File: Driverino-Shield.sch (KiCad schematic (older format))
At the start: 56 parts, among them P1 Power, P10 MOT, P11 HALL, P2 Analog, P3 Digital, P4 Digital, P5 CONN_01X01, P6 CONN_01X01, P7 CONN_01X01, P8 CONN_01X01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

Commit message: Update BOM
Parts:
- JP1: RS (none) -> 180-0478
- JP2: RS (none) -> 180-0534
- P11: RS (none) -> 279-9241
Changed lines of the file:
@@
 F 6 "Molex" H 15100 6950 50  0001 C CNN "Manufacturer"
 F 7 "538-53047-0810" H 15100 6950 50  0001 C CNN "Mouser"
+F 8 "279-9241" H 15100 6950 50  0001 C CNN "RS"
 	1    15100 6950
 	1    0    0    1
@@
 F 6 "Samtec" H 14700 5700 50  0001 C CNN "Manufacturer"
 F 7 "200-TMS10301GS" H 14700 5700 50  0001 C CNN "Mouser"
+F 8 "180-0478" H 14700 5700 50  0001 C CNN "RS"
 	1    14700 5700
 	1    0    0    -1
@@
 F 6 "Samtec" H 12250 4625 50  0001 C CNN "Manufacturer"
 F 7 "200-TMS10201GS" H 12250 4625 50  0001 C CNN "Mouser"
+F 8 "180-0534" H 12250 4625 50  0001 C CNN "RS"
 	1    12250 4625
 	1    0    0    -1

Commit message: Update BOM
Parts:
- C1: Digikey (none) -> 399-7444-1-ND
- C10, C11, C12, C4: Digikey (none) -> 445-6901-1-ND
- C2: Digikey (none) -> P124837CT-ND
- C3: Digikey (none) -> 445-172483-1-ND
- C5, C7: Digikey (none) -> 311-2082-1-ND
- C6: Digikey (none) -> 490-4762-1-ND
- C8, C9: Digikey (none) -> 445-5666-1-ND
- D1: Digikey (none) -> 475-2486-1-ND
- D2: Digikey (none) -> LBQ39G-N1OO-35-1-ND
- D3: Digikey (none) -> 475-3442-1-ND
- D5: Digikey (none) -> TSZU52C5V1RGG-ND
- F1: Digikey (none) -> 118-MF-ASML020/6-2DKR-ND
- JP1: Digikey (none) -> SAM10238-ND
- JP2: Digikey (none) -> SAM12199-ND
- L1: Digikey (none) -> CBC3225T470KRV
- P1, P4: Digikey (none) -> SSW-108-03-G-S-ND
- P10: Digikey (none) -> 0397730003-ND
- P11: Digikey (none) -> WM1737-ND
- P2: Digikey (none) -> SSW-106-03-G-S-ND
- P3: Digikey (none) -> SSW-110-03-G-S-ND
- P9: Digikey (none) -> 0397730002-ND
- R1, R13, R3, R5, R7, R8: Digikey (none) -> 541-3949-1-ND
- R10, R11, R12, R14, R15, R16, R17, R9: Digikey (none) -> 541-4013-1-ND
- R18, R19, R20, R21, R22, R23: Digikey (none) -> 541-3958-1-ND
- R2, R4, R6: Digikey (none) -> ESR03EZPF5101-ND

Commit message: Update BOM
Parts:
- C1: Farnell (none) -> 2118135RL
- C10, C11, C12, C4: Farnell (none) -> 2210830
- C2: Farnell (none) -> 3126986
- C3: Farnell (none) -> 2547055
- C5, C7: Farnell (none) -> 2211179
- C6: Farnell (none) -> 2470416
- C8, C9: Farnell (none) -> 2346967
- D4: Farnell (none) -> 2463989
- F1: Farnell (none) -> 3350793
- JP1: Farnell (none) -> 2856614
- JP2: Farnell (none) -> 2505048
- P11: Farnell (none) -> 1012258
- P3: Farnell (none) -> 3661270
- R18, R19, R20, R21, R22, R23: Farnell (none) -> 2616725
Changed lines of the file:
@@
 F 7 "200-SSW11003GS" H 14850 1600 50  0001 C CNN "Mouser"
 F 8 "SSW-110-03-G-S-ND" H 14850 1600 50  0001 C CNN "Digikey"
+F 9 "3661270" H 14850 1600 50  0001 C CNN "Farnell"
 	1    14850 1600
 	-1   0    0    -1
@@
 F 8 "81-GCM155R71H103KA5D" H 5150 4725 50  0001 C CNN "Mouser"
 F 9 "490-4762-1-ND" H 5150 4725 50  0001 C CNN "Digikey"
+F 10 "2470416" H 5150 4725 50  0001 C CNN "Farnell"
 	1    5150 4725
 	0    1    1    0
@@
 F 8 "603-CC603KRX7R9BB105" H 4475 4825 50  0001 C CNN "Mouser"
 F 9 "311-2082-1-ND" H 4475 4825 50  0001 C CNN "Digikey"
+F 10 "2211179" H 4475 4825 50  0001 C CNN "Farnell"
 	1    4475 4825
 	0    1    1    0
@@
 F 8 "810-CGA5L1X7R1V106KE" H 4075 5450 50  0001 C CNN "Mouser"
 F 9 "	445-172483-1-ND" H 4075 5450 50  0001 C CNN "Digikey"
+F 10 "2547055" H 4075 5450 50  0001 C CNN "Farnell"
 	1    4075 5450
 	-1   0    0    1
@@
 F 8 "810-CGA2B3X7R1V104K" H 4475 5450 50  0001 C CNN "Mouser"
 F 9 "445-6901-1-ND" H 4475 5450 50  0001 C CNN "Digikey"
+F 10 "2210830" H 4475 5450 50  0001 C CNN "Farnell"
 	1    4475 5450
 	-1   0    0    1
@@
 F 7 "667-EEE-FTV151XAV" H 3800 5450 50  0001 C CNN "Mouser"
 F 8 "	P124837CT-ND" H 3800 5450 50  0001 C CNN "Digikey"
+F 9 "	3126986" H 3800 5450 50  0001 C CNN "Farnell"
 	1    3800 5450
 	1    0    0    -1
@@
 F 8 "603-CC603KRX7R9BB105" H 7750 4825 50  0001 C CNN "Mouser"
 F 9 "311-2082-1-ND" H 7750 4825 50  0001 C CNN "Digikey"
+F 10 "2211179" H 7750 4825 50  0001 C CNN "Farnell"
 	1    7750 4825
 	0    -1   -1   0
@@
 F 9 "810-CGA2B3X7R1V104K" H 13050 6425 50  0001 C CNN "Mouser"
 F 10 "445-6901-1-ND" H 13050 6425 50  0001 C CNN "Digikey"
+F 11 "2210830" H 13050 6425 50  0001 C CNN "Farnell"
 	1    13050 6425
 	-1   0    0    1
@@
 F 9 "810-CGA2B3X7R1V104K" H 13050 6950 50  0001 C CNN "Mouser"
 F 10 "445-6901-1-ND" H 13050 6950 50  0001 C CNN "Digikey"
+F 11 "2210830" H 13050 6950 50  0001 C CNN "Farnell"
 	1    13050 6950
 	-1   0    0    1
@@
 F 9 "810-CGA2B3X7R1V104K" H 13050 7475 50  0001 C CNN "Mouser"
 F 10 "445-6901-1-ND" H 13050 7475 50  0001 C CNN "Digikey"
+F 11 "2210830" H 13050 7475 50  0001 C CNN "Farnell"
 	1    13050 7475
 	-1   0    0    1
@@
 F 7 "652-MF-ASML020/6-2" H 3150 8700 50  0001 C CNN "Mouser"
 F 8 "118-MF-ASML020/6-2DKR-ND" H 3150 8700 50  0001 C CNN "Digikey"
+F 9 "3350793" H 3150 8700 50  0001 C CNN "Farnell"
 	1    3150 8700
 	1    0    0    -1
@@
 F 8 "80-C1206C226M8R" H 3575 9075 50  0001 C CNN "Mouser"
 F 9 "	399-7444-1-ND" H 3575 9075 50  0001 C CNN "Digikey"
+F 10 "2118135RL" H 3575 9075 50  0001 C CNN "Farnell"
 	1    3575 9075
 	-1   0    0    1
@@
 F 6 "Kingbright " H 6650 9200 50  0001 C CNN "Manufacturer"
 F 7 "466-3728" H 6650 9200 50  0001 C CNN "RS"
+F 8 "2463989" H 6650 9200 50  0001 C CNN "Farnell"
 	1    6650 9200
 	0    1    1    0
@@
 F 8 "279-9241" H 15100 6950 50  0001 C CNN "RS"
 F 9 "WM1737-ND" H 15100 6950 50  0001 C CNN "Digikey"
+F 10 "1012258" H 15100 6950 50  0001 C CNN "Farnell"
 	1    15100 6950
 	1    0    0    1
@@
 F 8 "71-CRCW040210K0JNEDC" H 14225 7550 50  0001 C CNN "Mouser"
 F 9 "541-3958-1-ND" H 14225 7550 50  0001 C CNN "Digikey"
+F 10 "2616725" H 14225 7550 50  0001 C CNN "Farnell"
 	1    14225 7550
 	1    0    0    -1
@@
 F 8 "71-CRCW040210K0JNEDC" H 13950 7550 50  0001 C CNN "Mouser"
 F 9 "541-3958-1-ND" H 13950 7550 50  0001 C CNN "Digikey"
+F 10 "2616725" H 13950 7550 50  0001 C CNN "Farnell"
 	1    13950 7550
 	1    0    0    -1
@@
 F 8 "71-CRCW040210K0JNEDC" H 14500 7550 50  0001 C CNN "Mouser"
 F 9 "541-3958-1-ND" H 14500 7550 50  0001 C CNN "Digikey"
+F 10 "2616725" H 14500 7550 50  0001 C CNN "Farnell"
 	1    14500 7550
 	1    0    0    -1
@@
 F 8 "71-CRCW040210K0JNEDC" H 14500 6275 50  0001 C CNN "Mouser"
 F 9 "541-3958-1-ND" H 14500 6275 50  0001 C CNN "Digikey"
+F 10 "2616725" H 14500 6275 50  0001 C CNN "Farnell"
 	1    14500 6275
 	1    0    0    1
@@
 F 8 "71-CRCW040210K0JNEDC" H 14225 6275 50  0001 C CNN "Mouser"
 F 9 "541-3958-1-ND" H 14225 6275 50  0001 C CNN "Digikey"
+F 10 "2616725" H 14225 6275 50  0001 C CNN "Farnell"
 	1    14225 6275
 	1    0    0    1
@@
 F 8 "71-CRCW040210K0JNEDC" H 13950 6275 50  0001 C CNN "Mouser"
 F 9 "541-3958-1-ND" H 13950 6275 50  0001 C CNN "Digikey"
+F 10 "2616725" H 13950 6275 50  0001 C CNN "Farnell"
 	1    13950 6275
 	1    0    0    1
@@
 F 8 "10-CGA3E2X7R1H104K" H 8625 9075 50  0001 C CNN "Mouser"
 F 9 "445-5666-1-ND" H 8625 9075 50  0001 C CNN "Digikey"
+F 10 "2346967" H 8625 9075 50  0001 C CNN "Farnell"
 	1    8625 9075
 	-1   0    0    1
@@
 F 8 "10-CGA3E2X7R1H104K" H 10450 9075 50  0001 C CNN "Mouser"
 F 9 "445-5666-1-ND" H 10450 9075 50  0001 C CNN "Digikey"
+F 10 "2346967" H 10450 9075 50  0001 C CNN "Farnell"
 	1    10450 9075
 	-1   0    0    1
@@
 F 8 "180-0478" H 14700 5700 50  0001 C CNN "RS"
 F 9 "	SAM10238-ND" H 14700 5700 50  0001 C CNN "Digikey"
+F 10 "2856614" H 14700 5700 50  0001 C CNN "Farnell"
 	1    14700 5700
 	1    0    0    -1
@@
 F 8 "180-0534" H 12250 4625 50  0001 C CNN "RS"
 F 9 "SAM12199-ND" H 12250 4625 50  0001 C CNN "Digikey"
+F 10 "2505048" H 12250 4625 50  0001 C CNN "Farnell"
 	1    12250 4625
 	1    0    0    -1

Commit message: Update BOM
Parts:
- C2: manufacturer1 (none) -> Panasonic; mpn1 (none) -> EEEFTV151XAP
- D4: manufacturer1 (none) -> OSRAM Opto; mpn1 (none) -> LS Q976-NR-1
- D5: RS (none) -> 796-5676; manufacturer1 (none) -> Taiwan Semiconductor; mpn1 (none) -> BZT52C5V1K RKG
- P1, P4: RS (none) -> 180-0432; manufacturer1 (none) -> Samtec; mpn1 (none) -> SSW-108-03-T-S
- P2: RS (none) -> 180-0391; manufacturer1 (none) -> Samtec; mpn1 (none) -> SSW-106-03-T-S
- P3: RS (none) -> 207-9189; manufacturer1 (none) -> Samtec; mpn1 (none) -> SSW-110-03-T-S
- R1, R13, R3, R5, R7, R8: RS (none) -> 678-9875
- R10, R11, R12, R14, R15, R16, R17, R9: RS (none) -> 678-9670
- R18, R19, R20, R21, R22, R23: RS (none) -> 812-1723; manufacturer1 (none) -> Vishay; mpn1 (none) -> CRCW040210K0JNEDIF
- R2, R4, R6: RS (none) -> 679-0566; manufacturer1 (none) -> Vishay; mpn1 (none) -> CRCW06035K10FKEA
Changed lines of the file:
@@
 F 7 "200-SSW10803GS" H 14450 1900 50  0001 C CNN "Mouser"
 F 8 "SSW-108-03-G-S-ND" H 14450 1900 50  0001 C CNN "Digikey"
+F 9 "180-0432" H 14450 1900 50  0001 C CNN "RS"
+F 10 "Samtec" H 14450 1900 50  0001 C CNN "manufacturer1"
+F 11 "SSW-108-03-T-S" H 14450 1900 50  0001 C CNN "mpn1"
 	1    14450 1900
 	1    0    0    -1
@@
 F 7 "200-SSW10603GS" H 14450 2700 50  0001 C CNN "Mouser"
 F 8 "SSW-106-03-G-S-ND" H 14450 2700 50  0001 C CNN "Digikey"
+F 9 "180-0391" H 14450 2700 50  0001 C CNN "RS"
+F 10 "Samtec" H 14450 2700 50  0001 C CNN "manufacturer1"
+F 11 "SSW-106-03-T-S" H 14450 2700 50  0001 C CNN "mpn1"
 	1    14450 2700
 	1    0    0    -1
@@
 F 7 "200-SSW10803GS" H 14850 2600 50  0001 C CNN "Mouser"
 F 8 "SSW-108-03-G-S-ND" H 14850 2600 50  0001 C CNN "Digikey"
+F 9 "180-0432" H 14850 2600 50  0001 C CNN "RS"
+F 10 "Samtec" H 14850 2600 50  0001 C CNN "manufacturer1"
+F 11 "SSW-108-03-T-S" H 14850 2600 50  0001 C CNN "mpn1"
 	1    14850 2600
 	-1   0    0    -1
@@
 F 8 "SSW-110-03-G-S-ND" H 14850 1600 50  0001 C CNN "Digikey"
 F 9 "3661270" H 14850 1600 50  0001 C CNN "Farnell"
+F 10 "207-9189" H 14850 1600 50  0001 C CNN "RS"
+F 11 "Samtec" H 14850 1600 50  0001 C CNN "manufacturer1"
+F 12 "SSW-110-03-T-S" H 14850 1600 50  0001 C CNN "mpn1"
 	1    14850 1600
 	-1   0    0    -1
@@
 F 7 "755-ESR03EZPF5101" H 6925 2975 50  0001 C CNN "Mouser"
 F 8 "	ESR03EZPF5101-ND" H 6925 2975 50  0001 C CNN "Digikey"
+F 9 "679-0566" H 6925 2975 50  0001 C CNN "RS"
+F 10 "Vishay" H 6925 2975 50  0001 C CNN "manufacturer1"
+F 11 "CRCW06035K10FKEA" H 6925 2975 50  0001 C CNN "mpn1"
 	1    6925 2975
 	1    0    0    -1
@@
 F 8 "	P124837CT-ND" H 3800 5450 50  0001 C CNN "Digikey"
 F 9 "	3126986" H 3800 5450 50  0001 C CNN "Farnell"
+F 10 "Panasonic" H 3800 5450 50  0001 C CNN "manufacturer1"
+F 11 "EEEFTV151XAP" H 3800 5450 50  0001 C CNN "mpn1"
 	1    3800 5450
 	1    0    0    -1
@@
 F 7 "755-ESR03EZPF5101" H 5675 2975 50  0001 C CNN "Mouser"
 F 8 "	ESR03EZPF5101-ND" H 5675 2975 50  0001 C CNN "Digikey"
+F 9 "679-0566" H 5675 2975 50  0001 C CNN "RS"
+F 10 "Vishay" H 5675 2975 50  0001 C CNN "manufacturer1"
+F 11 "CRCW06035K10FKEA" H 5675 2975 50  0001 C CNN "mpn1"
 	1    5675 2975
 	-1   0    0    -1
@@
 F 7 "71-CRCW06031K00FKEAC" H 5200 8625 50  0001 C CNN "Mouser"
 F 8 "541-3949-1-ND" H 5200 8625 50  0001 C CNN "Digikey"
+F 9 "678-9875" H 5200 8625 50  0001 C CNN "RS"
 	1    5200 8625
 	1    0    0    -1
@@
 F 7 "71-CRCW06031K00FKEAC" H 5675 8625 50  0001 C CNN "Mouser"
 F 8 "541-3949-1-ND" H 5675 8625 50  0001 C CNN "Digikey"
+F 9 "678-9875" H 5675 8625 50  0001 C CNN "RS"
 	1    5675 8625
 	1    0    0    -1
@@
 F 7 "755-ESR03EZPF5101" H 6150 8625 50  0001 C CNN "Mouser"
 F 8 "	ESR03EZPF5101-ND" H 6150 8625 50  0001 C CNN "Digikey"
+F 9 "679-0566" H 6150 8625 50  0001 C CNN "RS"
+F 10 "Vishay" H 6150 8625 50  0001 C CNN "manufacturer1"
+F 11 "CRCW06035K10FKEA" H 6150 8625 50  0001 C CNN "mpn1"
 	1    6150 8625
 	1    0    0    -1
@@
 F 7 "71-CRCW06031K00FKEAC" H 6650 8625 50  0001 C CNN "Mouser"
 F 8 "541-3949-1-ND" H 6650 8625 50  0001 C CNN "Digikey"
+F 9 "678-9875" H 6650 8625 50  0001 C CNN "RS"
 	1    6650 8625
 	1    0    0    -1
@@
 F 7 "466-3728" H 6650 9200 50  0001 C CNN "RS"
 F 8 "2463989" H 6650 9200 50  0001 C CNN "Farnell"
+F 9 "OSRAM Opto" H 6650 9200 50  0001 C CNN "manufacturer1"
+F 10 "LS Q976-NR-1" H 6650 9200 50  0001 C CNN "mpn1"
 	1    6650 9200
 	0    1    1    0
@@
 F 7 "71-CRCW06030000Z0EBC" H 13875 4625 50  0001 C CNN "Mouser"
 F 8 "541-4013-1-ND" H 13875 4625 50  0001 C CNN "Digikey"
+F 9 "678-9670" H 13875 4625 50  0001 C CNN "RS"
 	1    13875 4625
 	0    1    1    0
@@
 F 9 "541-3958-1-ND" H 14225 7550 50  0001 C CNN "Digikey"
 F 10 "2616725" H 14225 7550 50  0001 C CNN "Farnell"
+F 11 "812-1723" H 14225 7550 50  0001 C CNN "RS"
+F 12 "Vishay" H 14225 7550 50  0001 C CNN "manufacturer1"
+F 13 "CRCW040210K0JNEDIF" H 14225 7550 50  0001 C CNN "mpn1"
 	1    14225 7550
 	1    0    0    -1
@@
 F 9 "541-3958-1-ND" H 13950 7550 50  0001 C CNN "Digikey"
 F 10 "2616725" H 13950 7550 50  0001 C CNN "Farnell"
+F 11 "812-1723" H 13950 7550 50  0001 C CNN "RS"
+F 12 "Vishay" H 13950 7550 50  0001 C CNN "manufacturer1"
+F 13 "CRCW040210K0JNEDIF" H 13950 7550 50  0001 C CNN "mpn1"
 	1    13950 7550
 	1    0    0    -1
@@
 F 9 "541-3958-1-ND" H 14500 7550 50  0001 C CNN "Digikey"
 F 10 "2616725" H 14500 7550 50  0001 C CNN "Farnell"
+F 11 "812-1723" H 14500 7550 50  0001 C CNN "RS"
+F 12 "Vishay" H 14500 7550 50  0001 C CNN "manufacturer1"
+F 13 "CRCW040210K0JNEDIF" H 14500 7550 50  0001 C CNN "mpn1"
 	1    14500 7550
 	1    0    0    -1
@@
 F 9 "541-3958-1-ND" H 14500 6275 50  0001 C CNN "Digikey"
 F 10 "2616725" H 14500 6275 50  0001 C CNN "Farnell"
+F 11 "812-1723" H 14500 6275 50  0001 C CNN "RS"
+F 12 "Vishay" H 14500 6275 50  0001 C CNN "manufacturer1"
+F 13 "CRCW040210K0JNEDIF" H 14500 6275 50  0001 C CNN "mpn1"
 	1    14500 6275
 	1    0    0    1
@@
 F 9 "541-3958-1-ND" H 14225 6275 50  0001 C CNN "Digikey"
 F 10 "2616725" H 14225 6275 50  0001 C CNN "Farnell"
+F 11 "812-1723" H 14225 6275 50  0001 C CNN "RS"
+F 12 "Vishay" H 14225 6275 50  0001 C CNN "manufacturer1"
+F 13 "CRCW040210K0JNEDIF" H 14225 6275 50  0001 C CNN "mpn1"
 	1    14225 6275
 	1    0    0    1
@@
 F 9 "541-3958-1-ND" H 13950 6275 50  0001 C CNN "Digikey"
 F 10 "2616725" H 13950 6275 50  0001 C CNN "Farnell"
+F 11 "812-1723" H 13950 6275 50  0001 C CNN "RS"
+F 12 "Vishay" H 13950 6275 50  0001 C CNN "manufacturer1"
+F 13 "CRCW040210K0JNEDIF" H 13950 6275 50  0001 C CNN "mpn1"
 	1    13950 6275
 	1    0    0    1
@@
 F 7 "71-CRCW06031K00FKEAC" H 8300 9075 50  0001 C CNN "Mouser"
 F 8 "541-3949-1-ND" H 8300 9075 50  0001 C CNN "Digikey"
+F 9 "678-9875" H 8300 9075 50  0001 C CNN "RS"
 	1    8300 9075
 	1    0    0    -1
@@
 F 7 "71-CRCW06031K00FKEAC" H 7950 8700 50  0001 C CNN "Mouser"
 F 8 "541-3949-1-ND" H 7950 8700 50  0001 C CNN "Digikey"
+F 9 "678-9875" H 7950 8700 50  0001 C CNN "RS"
 	1    7950 8700
 	0    1    1    0
@@
 F 7 "71-CRCW06031K00FKEAC" H 10100 8700 50  0001 C CNN "Mouser"
 F 8 "541-3949-1-ND" H 10100 8700 50  0001 C CNN "Digikey"
+F 9 "678-9875" H 10100 8700 50  0001 C CNN "RS"
 	1    10100 8700
 	0    1    1    0
@@
 F 7 "71-CRCW06030000Z0EBC" H 10200 4850 50  0001 C CNN "Mouser"
 F 8 "541-4013-1-ND" H 10200 4850 50  0001 C CNN "Digikey"
+F 9 "678-9670" H 10200 4850 50  0001 C CNN "RS"
 	1    10200 4850
 	0    1    1    0
@@
 F 7 "71-CRCW06030000Z0EBC" H 10200 4550 50  0001 C CNN "Mouser"
 F 8 "541-4013-1-ND" H 10200 4550 50  0001 C CNN "Digikey"
+F 9 "678-9670" H 10200 4550 50  0001 C CNN "RS"
 	1    10200 4550
 	0    1    1    0
@@
 F 7 "71-CRCW06030000Z0EBC" H 10200 5150 50  0001 C CNN "Mouser"
 F 8 "541-4013-1-ND" H 10200 5150 50  0001 C CNN "Digikey"
+F 9 "678-9670" H 10200 5150 50  0001 C CNN "RS"
 	1    10200 5150
 	0    1    1    0
@@
 F 7 "71-CRCW06030000Z0EBC" H 10200 5800 50  0001 C CNN "Mouser"
 F 8 "541-4013-1-ND" H 10200 5800 50  0001 C CNN "Digikey"
+F 9 "678-9670" H 10200 5800 50  0001 C CNN "RS"
 	1    10200 5800
 	0    1    1    0
@@
 F 7 "71-CRCW06030000Z0EBC" H 10200 6425 50  0001 C CNN "Mouser"
 F 8 "541-4013-1-ND" H 10200 6425 50  0001 C CNN "Digikey"
+F 9 "678-9670" H 10200 6425 50  0001 C CNN "RS"
 	1    10200 6425
 	0    1    1    0
@@
 F 7 "71-CRCW06030000Z0EBC" H 10200 5475 50  0001 C CNN "Mouser"
 F 8 "541-4013-1-ND" H 10200 5475 50  0001 C CNN "Digikey"
+F 9 "678-9670" H 10200 5475 50  0001 C CNN "RS"
 	1    10200 5475
 	0    1    1    0
@@
 F 7 "71-CRCW06030000Z0EBC" H 10200 6125 50  0001 C CNN "Mouser"
 F 8 "541-4013-1-ND" H 10200 6125 50  0001 C CNN "Digikey"
+F 9 "678-9670" H 10200 6125 50  0001 C CNN "RS"
 	1    10200 6125
 	0    1    1    0
@@
 F 7 "821-TSZU52C5V1RGG" H 9050 9075 50  0001 C CNN "Mouser"
 F 8 "	TSZU52C5V1RGG-ND" H 9050 9075 50  0001 C CNN "Digikey"
+F 9 "796-5676" H 9050 9075 50  0001 C CNN "RS"
+F 10 "Taiwan Semiconductor" H 9050 9075 50  0001 C CNN "manufacturer1"
+F 11 "BZT52C5V1K RKG" H 9050 9075 50  0001 C CNN "mpn1"
 	1    9050 9075
 	0    -1   -1   0

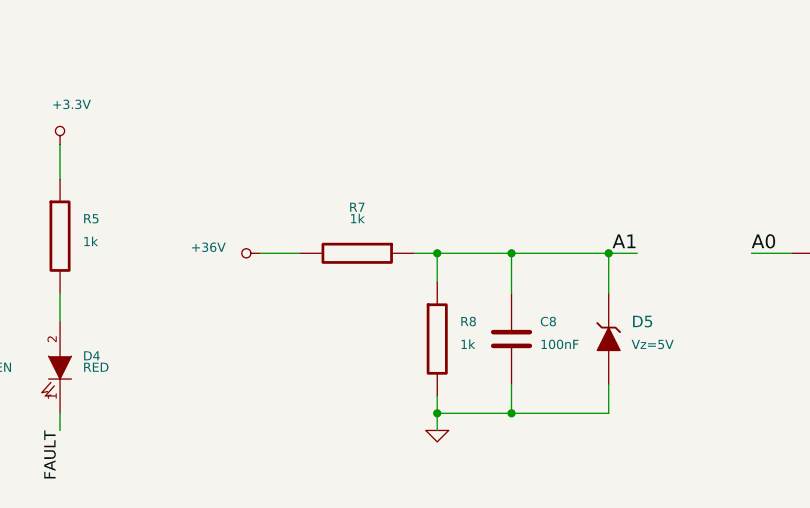
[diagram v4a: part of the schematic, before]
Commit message: Fixed VMOT input resistance partition, update BOM
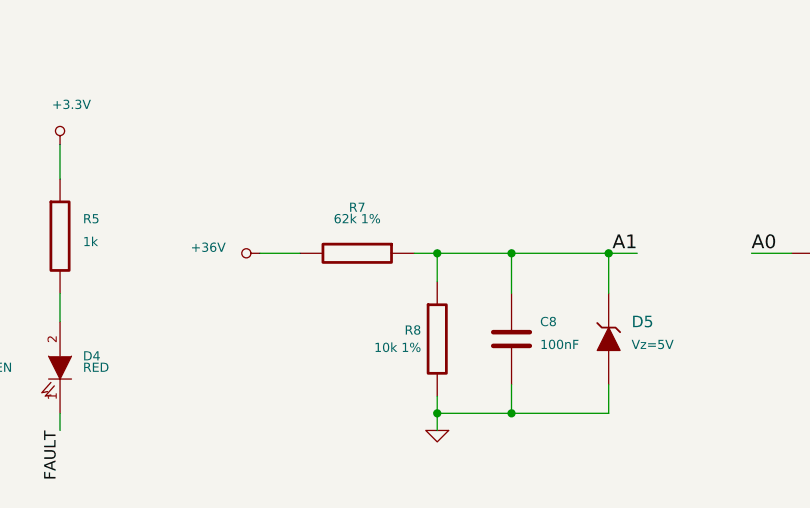
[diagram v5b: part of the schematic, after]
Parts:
- R7: value 1k -> 62k 1%; Digikey 541-3949-1-ND -> ERJ-3RBD6202V-ND; Farnell (none) -> 2380068; Manufacturer Vishay -> Panasonic; Mouser 71-CRCW06031K00FKEAC -> 667-ERJ-3RBD6202V; RS 678-9875 -> 810-2306; manf# CRCW06031K00FKEAC -> ERJ3RBD6202V; mpn CRCW06031K00FKEAC -> ERJ3RBD6202V
- R8: value 1k -> 10k 1%; Digikey 541-3949-1-ND -> 311-10.0KHRCT-ND; Farnell (none) -> 9238603; Manufacturer Vishay -> Yageo; Mouser 71-CRCW06031K00FKEAC -> 603-RC0603FR-0710KL; RS 678-9875 -> 199-5443; manf# CRCW06031K00FKEAC -> RC0603FR-0710KL; mpn CRCW06031K00FKEAC -> RC0603FR-0710KL
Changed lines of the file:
@@
 U 1 1 60BF2E41
 P 8300 9075
-F 0 "R8" H 8400 9150 40  0000 L CNN
-F 1 "1k" H 8400 9050 40  0000 L CNN
+F 0 "R8" H 8230 9113 40  0000 R CNN
+F 1 "10k 1%" H 8230 9037 40  0000 R CNN
 F 2 "Resistor_SMD:R_0603_1608Metric" V 8230 9075 30  0001 C CNN
-F 3 "" H 8300 9075 30  0000 C CNN
-F 4 "CRCW06031K00FKEAC" H 8300 9075 50  0001 C CNN "manf#"
-F 5 "CRCW06031K00FKEAC" H 8300 9075 50  0001 C CNN "mpn"
-F 6 "Vishay" H 8300 9075 50  0001 C CNN "Manufacturer"
-F 7 "71-CRCW06031K00FKEAC" H 8300 9075 50  0001 C CNN "Mouser"
-F 8 "541-3949-1-ND" H 8300 9075 50  0001 C CNN "Digikey"
-F 9 "678-9875" H 8300 9075 50  0001 C CNN "RS"
+F 3 "" H 8300 9075 30  0001 C CNN
+F 4 "RC0603FR-0710KL" H 8300 9075 50  0001 C CNN "manf#"
+F 5 "RC0603FR-0710KL" H 8300 9075 50  0001 C CNN "mpn"
+F 6 "Yageo" H 8300 9075 50  0001 C CNN "Manufacturer"
+F 7 "603-RC0603FR-0710KL" H 8300 9075 50  0001 C CNN "Mouser"
+F 8 "311-10.0KHRCT-ND" H 8300 9075 50  0001 C CNN "Digikey"
+F 9 "199-5443" H 8300 9075 50  0001 C CNN "RS"
+F 10 "" H 8300 9075 50  0001 C CNN "mpn1"
+F 11 "" H 8300 9075 50  0001 C CNN "Manufacturer1"
+F 12 "9238603" H 8300 9075 50  0001 C CNN "Farnell"
 	1    8300 9075
 	1    0    0    -1
@@
 P 7950 8700
 F 0 "R7" V 7750 8700 40  0000 C CNN
-F 1 "1k" V 7800 8700 40  0000 C CNN
+F 1 "62k 1%" V 7800 8700 40  0000 C CNN
 F 2 "Resistor_SMD:R_0603_1608Metric" V 7880 8700 30  0001 C CNN
-F 3 "" H 7950 8700 30  0000 C CNN
-F 4 "CRCW06031K00FKEAC" H 7950 8700 50  0001 C CNN "manf#"
-F 5 "CRCW06031K00FKEAC" H 7950 8700 50  0001 C CNN "mpn"
-F 6 "Vishay" H 7950 8700 50  0001 C CNN "Manufacturer"
-F 7 "71-CRCW06031K00FKEAC" H 7950 8700 50  0001 C CNN "Mouser"
-F 8 "541-3949-1-ND" H 7950 8700 50  0001 C CNN "Digikey"
-F 9 "678-9875" H 7950 8700 50  0001 C CNN "RS"
+F 3 "" H 7950 8700 30  0001 C CNN
+F 4 "ERJ3RBD6202V" H 7950 8700 50  0001 C CNN "manf#"
+F 5 "ERJ3RBD6202V" H 7950 8700 50  0001 C CNN "mpn"
+F 6 "Panasonic" H 7950 8700 50  0001 C CNN "Manufacturer"
+F 7 "667-ERJ-3RBD6202V" H 7950 8700 50  0001 C CNN "Mouser"
+F 8 "ERJ-3RBD6202V-ND" H 7950 8700 50  0001 C CNN "Digikey"
+F 9 "810-2306" H 7950 8700 50  0001 C CNN "RS"
+F 10 "2380068" V 7950 8700 50  0001 C CNN "Farnell"
 	1    7950 8700
 	0    1    1    0

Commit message: Changed F1 footprint, BOM update
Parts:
- F1: footprint Fuse:Fuse_0402_1005Metric -> Fuse:Fuse_1206_3216Metric_Castellated; Digikey 118-MF-ASML020/6-2DKR-ND -> MF-NSMF020-2CT-ND; Farnell 3350793 -> 1817286; Mouser 652-MF-ASML020/6-2 -> 652-MF-NSMF020-2; RS (none) -> 647-8279; manf# MF-ASML020/6-2 -> MF-NSMF020-2; mpn MF-ASML020/6-2 -> MF-NSMF020-2
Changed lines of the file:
@@
 F 0 "F1" H 3150 8950 40  0000 C CNN
 F 1 "200mA" H 3150 8850 40  0000 C CNN
-F 2 "Fuse:Fuse_0402_1005Metric" H 3150 8700 60  0001 C CNN
+F 2 "Fuse:Fuse_1206_3216Metric_Castellated" H 3150 8700 60  0001 C CNN
 F 3 "" H 3150 8700 60  0000 C CNN
-F 4 "MF-ASML020/6-2" H 3150 8700 50  0001 C CNN "manf#"
-F 5 "MF-ASML020/6-2" H 3150 8700 50  0001 C CNN "mpn"
+F 4 "MF-NSMF020-2" H 3150 8700 50  0001 C CNN "manf#"
+F 5 "MF-NSMF020-2" H 3150 8700 50  0001 C CNN "mpn"
 F 6 "Bourns" H 3150 8700 50  0001 C CNN "Manufacturer"
-F 7 "652-MF-ASML020/6-2" H 3150 8700 50  0001 C CNN "Mouser"
-F 8 "118-MF-ASML020/6-2DKR-ND" H 3150 8700 50  0001 C CNN "Digikey"
-F 9 "3350793" H 3150 8700 50  0001 C CNN "Farnell"
+F 7 "652-MF-NSMF020-2" H 3150 8700 50  0001 C CNN "Mouser"
+F 8 "MF-NSMF020-2CT-ND" H 3150 8700 50  0001 C CNN "Digikey"
+F 9 "1817286" H 3150 8700 50  0001 C CNN "Farnell"
+F 10 "647-8279" H 3150 8700 50  0001 C CNN "RS"
 	1    3150 8700
 	1    0    0    -1

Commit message: Update BOM
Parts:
- U1: manf# MCT8316Z -> PMCT8316Z0TRGFR; mpn MCT8316Z -> PMCT8316Z0TRGFR
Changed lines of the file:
@@
 F 2 "Driverino-Shield:QFN-40_EP_5x7_Pitch0.5mm" H 8225 4950 50  0001 C CNN
 F 3 "" H 8225 4950 50  0001 C CNN
-F 4 "MCT8316Z" H 6300 4675 50  0001 C CNN "manf#"
-F 5 "MCT8316Z" H 6300 4675 50  0001 C CNN "mpn"
+F 4 "PMCT8316Z0TRGFR" H 6300 4675 50  0001 C CNN "manf#"
+F 5 "PMCT8316Z0TRGFR" H 6300 4675 50  0001 C CNN "mpn"
 F 6 "TI" H 6300 4675 50  0001 C CNN "Manufacturer"
 	1    6300 4675
